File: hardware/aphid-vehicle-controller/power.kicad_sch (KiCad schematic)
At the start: 0 parts

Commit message: worked on schematic
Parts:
- added C15: 100uF, symbol Device:C_Polarized
- added C16: 10 uF, symbol Device:C_Polarized
- added C17, C18: 1 uF, symbol Device:C
- added C19, C20, C21: C, symbol Device:C
- added D5: B340, Diode_SMD:D_SMC, symbol Diode:B340
- added L3: 22 uH, symbol Device:L_Iron
- added R5, R6: R, symbol Device:R
- added U6: AMS1117-3.3, Package_TO_SOT_SMD:SOT-223-3_TabPin2, symbol Regulator_Linear:AMS1117-3.3
- added U7: TPS5430DDA, Package_SO:TI_SO-PowerPAD-8_ThermalVias, symbol Regulator_Switching:TPS5430DDA
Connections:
- net +3.3V: now also C20.1, U6.2 (VO)
- net +5V: now also C15.1, C17.1, C19.1, L3.2, R5.1, U6.3 (VI)
- net GND: now also C15.2, C17.2, C19.2, C20.2, D5.2 (A), R6.2, U6.1 (GND), U7.6 (GND), U7.9 (GNDPAD)
- new net: R5.2, R6.1, U7.4 (VSENSE)
- new net: C21.1, U7.1 (BOOT)
- new net: C21.2, D5.1 (K), L3.1, U7.8 (PH)
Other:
- note added: "TODO: Add some protection and filtering here"

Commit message: more work on pcb
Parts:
- removed C16: 10 uF, symbol Device:C_Polarized
- added C16, C27, C28, C29: 10 uF, symbol Device:C
- added C23, C25: 1uF, symbol Device:C
- added C26: 100nF, symbol Device:C
- added D6, D7: 3.6 V, symbol Device:D_Zener
- added D8: BAT54C, Package_TO_SOT_SMD:SOT-23, symbol Diode:BAT54C
- added L4, L5: L, symbol Device:L
- added R13, R19, R20: 10k, symbol Device:R
- added R14, R18, R21: 38k, symbol Device:R
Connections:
- net +12V: now also C18.1, U7.7 (VIN), C16.1, C27.1, C28.1, L4.2
- net +5V: now also L5.1
- net GND: now also C18.2, C16.2, C23.2, C25.2, C26.2, C27.2, C28.2, C29.2, D6.2 (A), D7.2 (A), R13.1, R19.1, R20.1
- net VIN: now also L4.1, R18.2
- net VIN_SENSE: now also C25.1, D7.1 (K), R18.1, R19.2
- net at U7.5 (EN): now also C26.1, D8.3, R20.2
- new net: D8.2, R21.1
- new net ACC_5V: C29.1, L5.2
- new net IGNITION: R14.2, R21.2
- new net IGNITION_SENSE: C23.1, D6.1 (K), R13.2, R14.1
- new net POWER_KEEPALIVE: D8.1
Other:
- note added: "5V Supply to the accelerator pedal Hall effect sensors"
- note added: "R1 = 38 kOhm R2 = 10 kOhm C = 1 uF Vin = 14 V Vout = ~3 V Fc = ~4 Hz"
- moved on the sheet: C15, C17, C18, C19, C20, C21, D5, L3, R5, R6, U6, U7

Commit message: worked on VCM
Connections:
- net ACC_5V renamed EXT_5V
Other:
- note added: "5V Supply to the accelerator pedal Hall effect sensors and direction selector switches"
- note removed: "5V Supply to the accelerator pedal Hall effect sensors"
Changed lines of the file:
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@@
 		)
 	)
-	(text "5V Supply to the accelerator \npedal Hall effect sensors"
+	(text "5V Supply to the accelerator \npedal Hall effect sensors and\ndirection selector switches"
 		(exclude_from_sim no)
 		(at 244.602 76.962 0)
@@
 		)
 	)
-	(hierarchical_label "ACC_5V"
+	(hierarchical_label "EXT_5V"
 		(shape output)
 		(at 233.68 71.12 0)
 		(fields_autoplaced yes)
 		(effects
+			(font
+				(size 1.27 1.27)
+			)
+			(justify left)
+		)
+	)
+	(hierarchical_label "CRANK"
+		(shape input)
+		(at 73.66 187.96 180)
+		(fields_autoplaced yes)
+		(effects
+			(font
+				(size 1.27 1.27)
+			)
+			(justify right)
+		)
+	)
+	(hierarchical_label "CRANK_SENSE"
+		(shape input)
+		(at 116.84 187.96 0)
+		(fields_autoplaced yes)
+		(effects

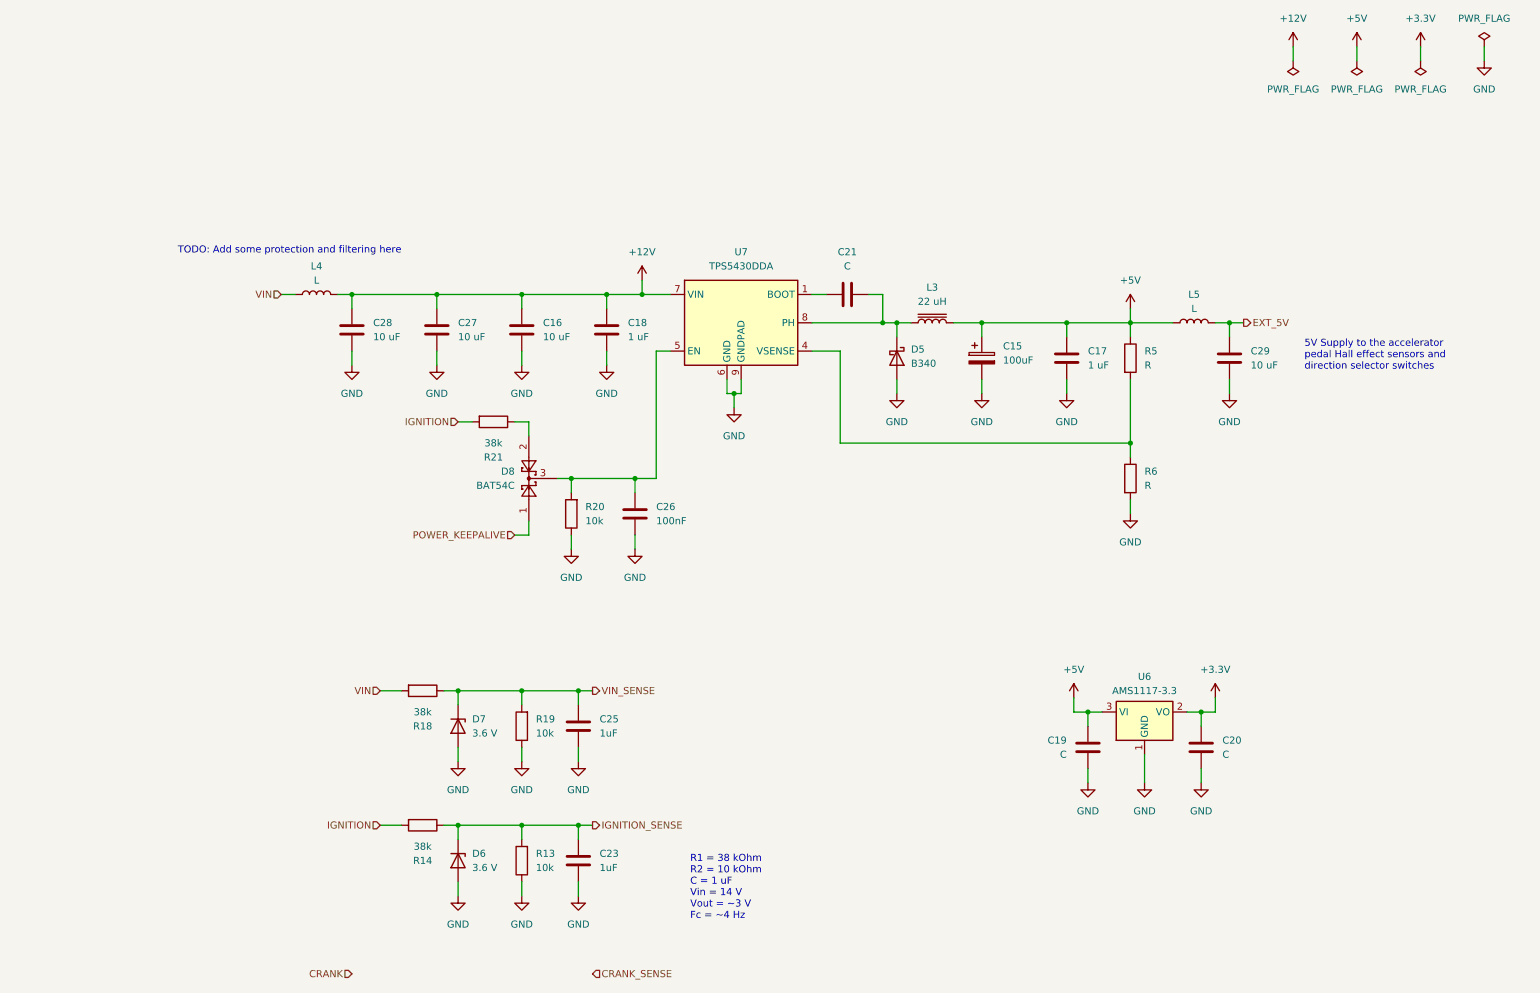
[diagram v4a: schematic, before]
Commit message: feat: changed to STM32G4xx series MCU
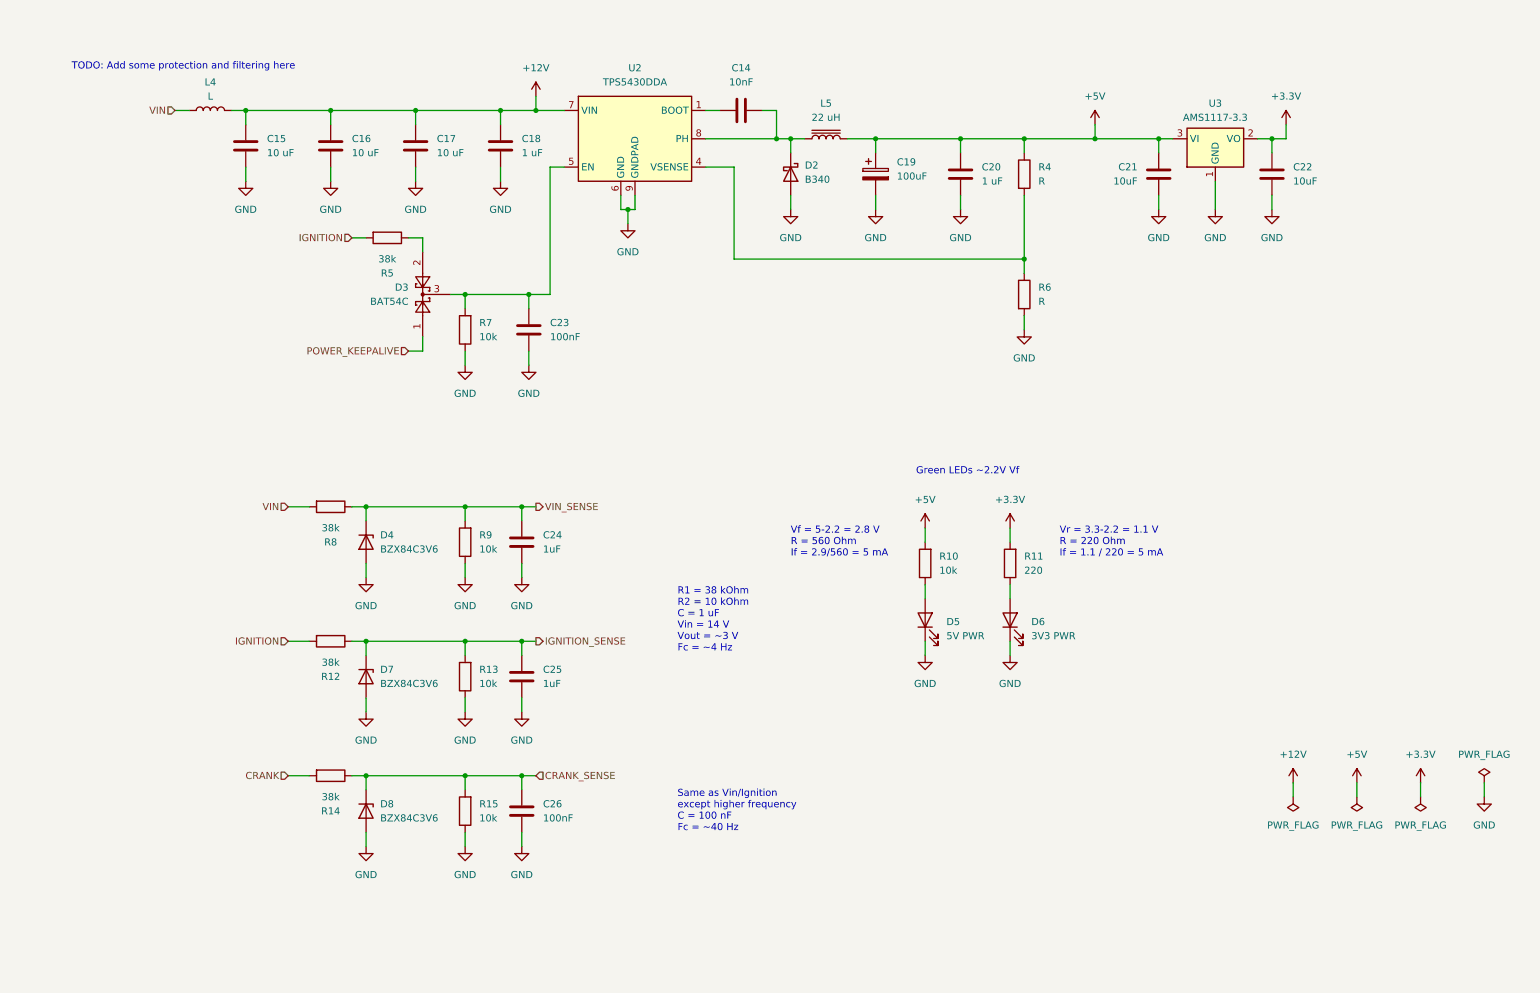
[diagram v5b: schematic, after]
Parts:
- removed C29: 10 uF, symbol Device:C
- removed D6, D7: 3.6 V, symbol Device:D_Zener
- removed L5: L, symbol Device:L
- added C26: 100nF, Capacitor_SMD:C_0603_1608Metric, symbol Device:C
- added D4, D7, D8: BZX84C3V6, Package_TO_SOT_SMD:SOT-23, symbol Diode:BZX84Cxx
- added D5: 5V PWR, LED_SMD:LED_0603_1608Metric, symbol Device:LED
- added D6: 3V3 PWR, LED_SMD:LED_0603_1608Metric, symbol Device:LED
- added R10, R15: 10k, Resistor_SMD:R_0603_1608Metric, symbol Device:R
- added R11: 220, Resistor_SMD:R_0603_1608Metric, symbol Device:R
- added R14: 38k, Resistor_SMD:R_0603_1608Metric, symbol Device:R
- C14: renamed from C21; value C -> 10nF; footprint (none) -> Capacitor_SMD:C_0603_1608Metric
- C15: renamed from C28; footprint (none) -> Capacitor_SMD:C_0805_2012Metric
- C16: renamed from C27; footprint (none) -> Capacitor_SMD:C_0805_2012Metric
- C17: renamed from C16; footprint (none) -> Capacitor_SMD:C_0805_2012Metric
- C18: footprint (none) -> Capacitor_SMD:C_0603_1608Metric
- C19: renamed from C15; footprint (none) -> Capacitor_SMD:C_0603_1608Metric
- C20: renamed from C17; footprint (none) -> Capacitor_SMD:C_0603_1608Metric
- C21: renamed from C19; value C -> 10uF; footprint (none) -> Capacitor_SMD:C_0805_2012Metric
- C22: renamed from C20; value C -> 10uF; footprint (none) -> Capacitor_SMD:C_0805_2012Metric
- C23: renamed from C26; footprint (none) -> Capacitor_SMD:C_0603_1608Metric
- C24: renamed from C25; footprint (none) -> Capacitor_SMD:C_0603_1608Metric
- C25: renamed from C23; footprint (none) -> Capacitor_SMD:C_0603_1608Metric
- L4: footprint (none) -> Inductor_SMD:L_Bourns_SRR1260
- L5: renamed from L3; footprint (none) -> Inductor_SMD:L_Bourns_SRR1260
- R12: renamed from R14; footprint (none) -> Resistor_SMD:R_0603_1608Metric
- R13, R6: footprint (none) -> Resistor_SMD:R_0603_1608Metric
- R4: renamed from R5; footprint (none) -> Resistor_SMD:R_0603_1608Metric
- R5: renamed from R21; footprint (none) -> Resistor_SMD:R_0603_1608Metric
- R7: renamed from R20; footprint (none) -> Resistor_SMD:R_0603_1608Metric
- R8: renamed from R18; footprint (none) -> Resistor_SMD:R_0603_1608Metric
- R9: renamed from R19; footprint (none) -> Resistor_SMD:R_0603_1608Metric
- renumbered D5 to D2, D8 to D3, U7 to U2, U6 to U3
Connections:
- net +3.3V: now also R11.2
- net +5V: now also R10.2
- net CRANK: now also R14.2
- net CRANK_SENSE: now also C26.1, D8.3 (K), R14.1, R15.2
- net GND: now also C26.2, D4.1 (A), D5.1 (K), D6.1 (K), D7.1 (A), D8.1 (A), R15.1
- net IGNITION_SENSE: now also D7.3 (K)
- net VIN_SENSE: now also D4.3 (K)
- new net: D6.2 (A), R11.1
- new net: D5.2 (A), R10.1
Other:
- note added: "Green LEDs ~2.2V Vf"
- note added: "Same as Vin/Ignition except higher frequency C = 100 nF Fc = ~40 Hz"
- note added: "Vf = 5-2.2 = 2.8 V R = 560 Ohm If = 2.9/560 = 5 mA"
- note added: "Vr = 3.3-2.2 = 1.1 V R = 220 Ohm If = 1.1 / 220 = 5 mA"
- note removed: "5V Supply to the accelerator pedal Hall effect sensors and direction selector switches"
- moved on the sheet: C14, C15, C16, C17, C18, C19, C20, C21, C22, C23, C24, C25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

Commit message: feat: changed to a more modern DCDC
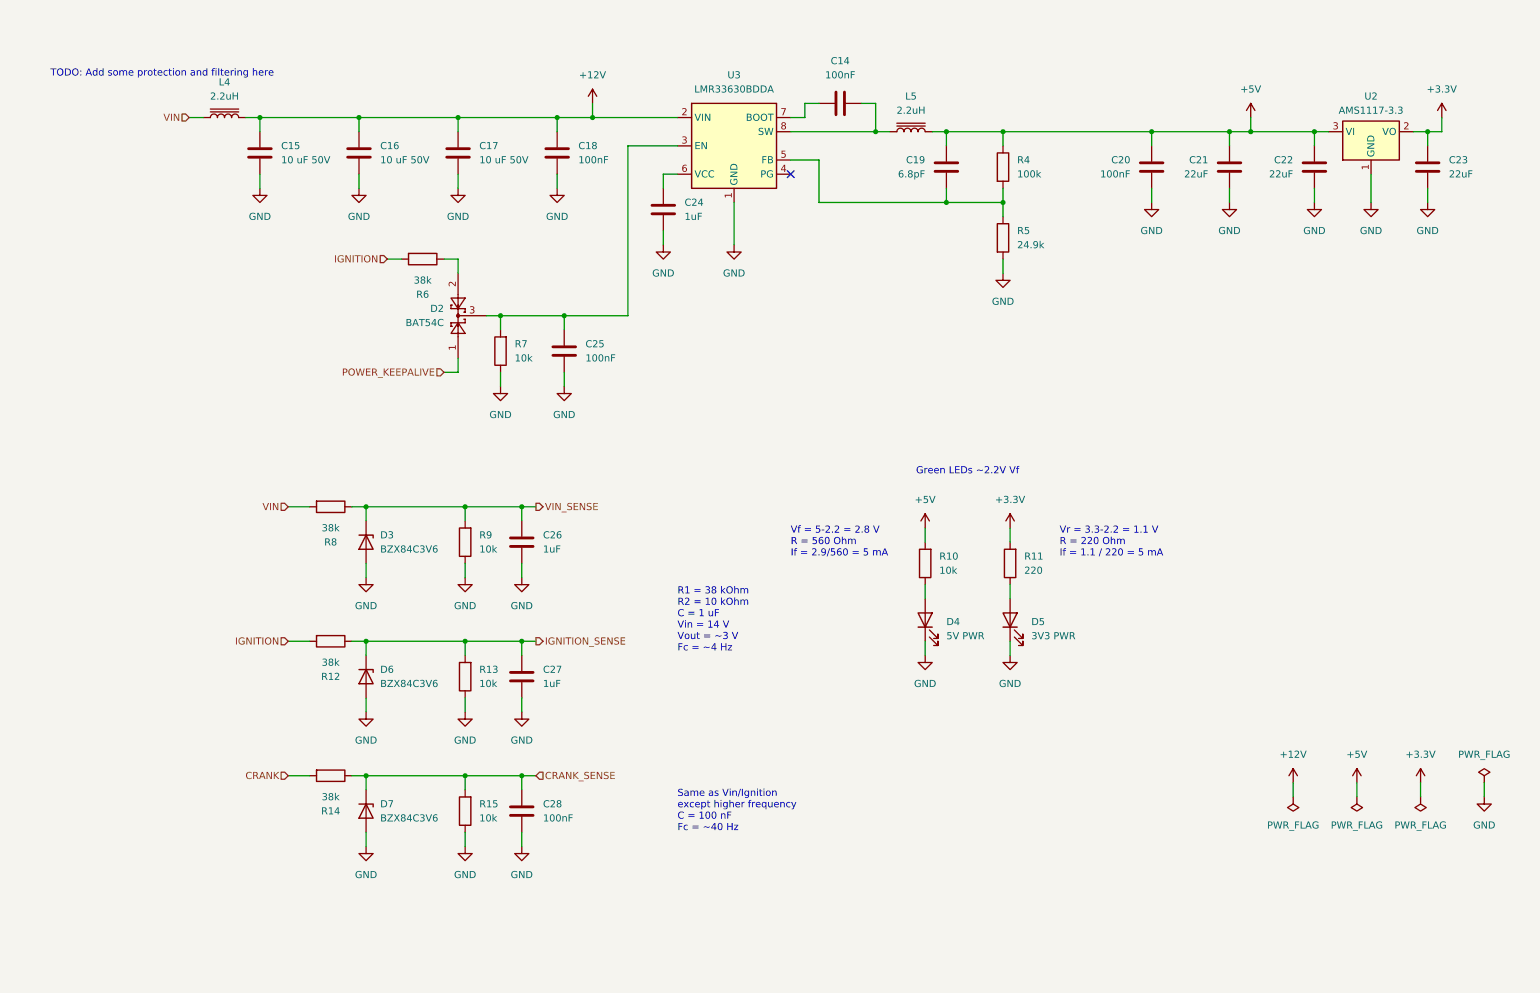
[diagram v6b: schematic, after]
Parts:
- removed C19: 100uF, Capacitor_SMD:C_0603_1608Metric, symbol Device:C_Polarized
- removed D2: B340, Diode_SMD:D_SMC, symbol Diode:B340
- removed L4: L, Inductor_SMD:L_Bourns_SRR1260, symbol Device:L
- removed U2: TPS5430DDA, Package_SO:TI_SO-PowerPAD-8_ThermalVias, symbol Regulator_Switching:TPS5430DDA
- added C19: 6.8pF, Capacitor_SMD:C_0603_1608Metric, symbol Device:C
- added C20: 100nF, Capacitor_SMD:C_0603_1608Metric, symbol Device:C
- added C21: 22uF, Capacitor_SMD:C_0805_2012Metric, symbol Device:C
- added L4: 2.2uH, Inductor_SMD:L_Bourns_SRN8040TA, symbol Device:L_Iron
- added U3: LMR33630BDDA, Package_SO:Texas_HSOP-8-1EP_3.9x4.9mm_P1.27mm_ThermalVias, symbol Regulator_Switching:LMR33630BDDA
- C14: value 10nF -> 100nF
- C15, C16, C17: value 10 uF -> 10 uF 50V; footprint Capacitor_SMD:C_0805_2012Metric -> Capacitor_SMD:C_1206_3216Metric
- C18: value 1 uF -> 100nF
- C22: renamed from C21; value 10uF -> 22uF
- C23: renamed from C22; value 10uF -> 22uF
- C24: renamed from C20; value 1 uF -> 1uF
- L5: value 22 uH -> 2.2uH; footprint Inductor_SMD:L_Bourns_SRR1260 -> Inductor_SMD:L_Bourns_SRN8040TA; Part (none) -> SRN8040-2R2Y
- R4: value R -> 100k
- R5: renamed from R6; value R -> 24.9k
- renumbered C23 to C25, C24 to C26, C25 to C27, C26 to C28, D3 to D2, D4 to D3, D5 to D4, D6 to D5, D7 to D6, D8 to D7, R5 to R6, U3 to U2
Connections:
- net +12V: now also L4.2, U3.2 (VIN)
- net +5V: now also C19.1, C20.1, C21.1; no longer C24.1
- net GND: now also C20.2, C21.2, U3.1 (GND), U3.9 (GND)
- net VIN: now also L4.1
- net at R4.2, R5.1: now also C19.2, U3.5 (FB)
- net at C14.1: now also U3.7 (BOOT)
- net at C25.1, D2.3, R7.2: now also U3.3 (EN)
- net at C14.2, L5.1: now also U3.8 (SW)
- new net: C24.1, U3.6 (VCC)
- no-connect marks 0 -> 1
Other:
- moved on the sheet: C14, C15, C22, C23, C24, C25, D2, L5, R4, R5, R6, R7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

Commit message: Worked on VC PCB
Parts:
- added C15, C19: 10 uF 50V, Capacitor_SMD:C_1206_3216Metric, symbol Device:C
- R7: value 10k -> 100k
- renumbered C15 to C16, C16 to C17, C17 to C18, C18 to C20, C19 to C21, C20 to C22, C21 to C23, C22 to C24, C23 to C25, C24 to C26, C25 to C27, C26 to C28, C27 to C29, C28 to C30
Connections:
- net +12V: now also C19.1; no longer C16.1
- net GND: now also C15.2, C19.2
- net POWER_KEEPALIVE: now also D2.2; no longer D2.1
- net VIN: now also C16.1, C15.1
- net at R6.1: now also D2.1; no longer D2.2
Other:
- note removed: "TODO: Add some protection and filtering here"
- moved on the sheet: C14, C16, C17, C18, C20, C21, C22, C23, C24, C25, C26, C27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
